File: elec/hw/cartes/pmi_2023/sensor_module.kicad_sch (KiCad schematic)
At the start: 25 parts, among them U12 LSM6DSO32XTR, U22 VL53L5CXV0GC, U30 VL53L5CXV0GC

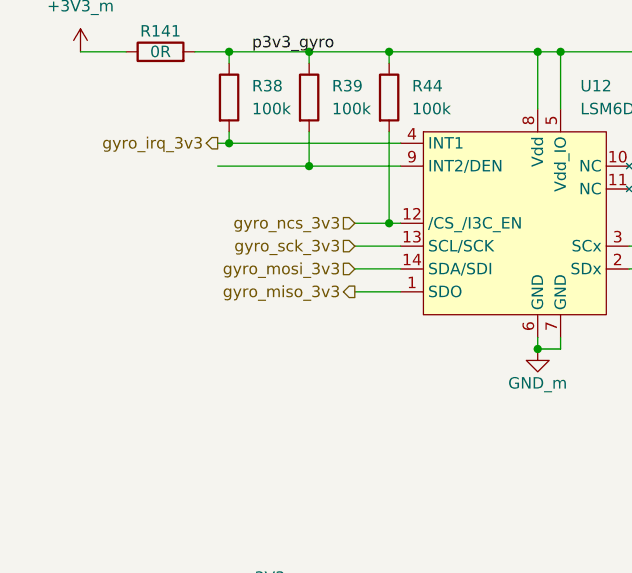
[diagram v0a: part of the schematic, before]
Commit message: GP2S60B replaced by ITR1204SR10A, RGB LED replaced by NH-B2020RGBA
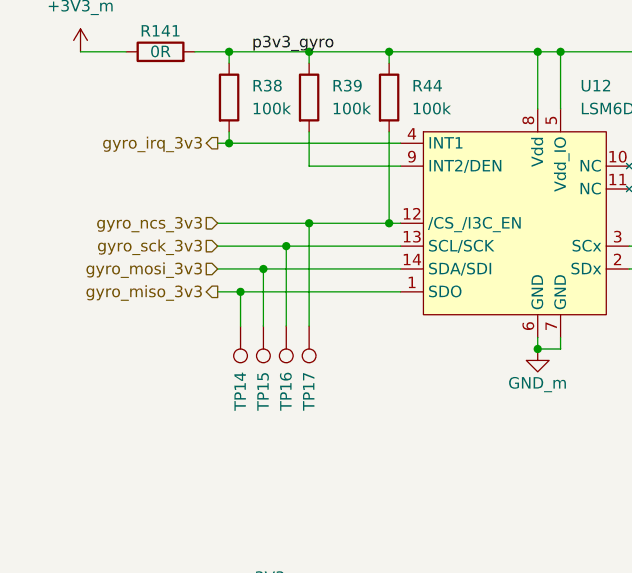
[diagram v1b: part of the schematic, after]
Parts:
- added TP14, TP15, TP16, TP17: TestPoint, cocotter_others:testpoint-THT-0.5mm, symbol cocotter_others:TestPoint
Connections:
- net gyro_miso_3v3: now also TP14.1
- net gyro_mosi_3v3: now also TP15.1
- net gyro_ncs_3v3: now also TP17.1
- net gyro_sck_3v3: now also TP16.1

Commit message: start sensor replaced
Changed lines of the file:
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@@
 					(size 1.27 1.27)
 				)
+				(hide yes)
 			)
 		)
@@
 		(on_board yes)
 		(dnp no)
-		(fields_autoplaced yes)
 		(property "Reference" "U12"
-			(at 73.3141 26.67 0)
+			(at 72.39 30.48 0)
 			(effects
 				(font
@@
 		)
 		(property "Value" "LSM6DSO32XTR"
-			(at 73.3141 29.21 0)
+			(at 72.39 53.34 0)
 			(effects
 				(font
@@
 					(size 1.27 1.27)
 				)
-			)
-		)
+				(hide yes)
+			)
+		)

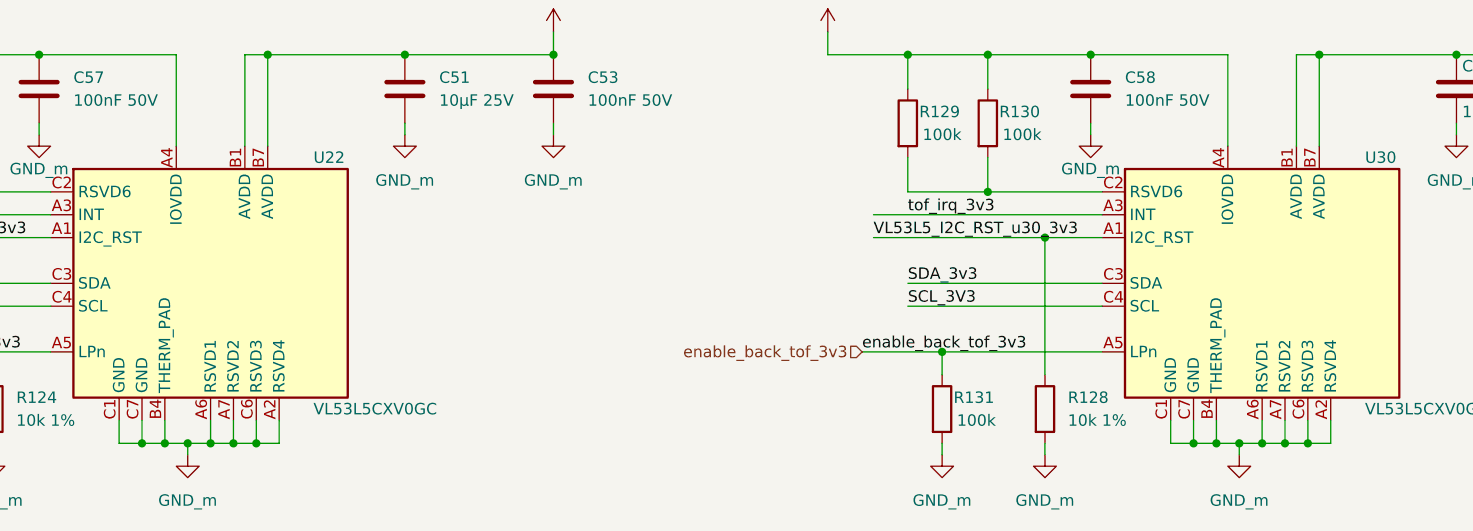
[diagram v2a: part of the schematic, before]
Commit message: XRA1200 replaced by TCA6408
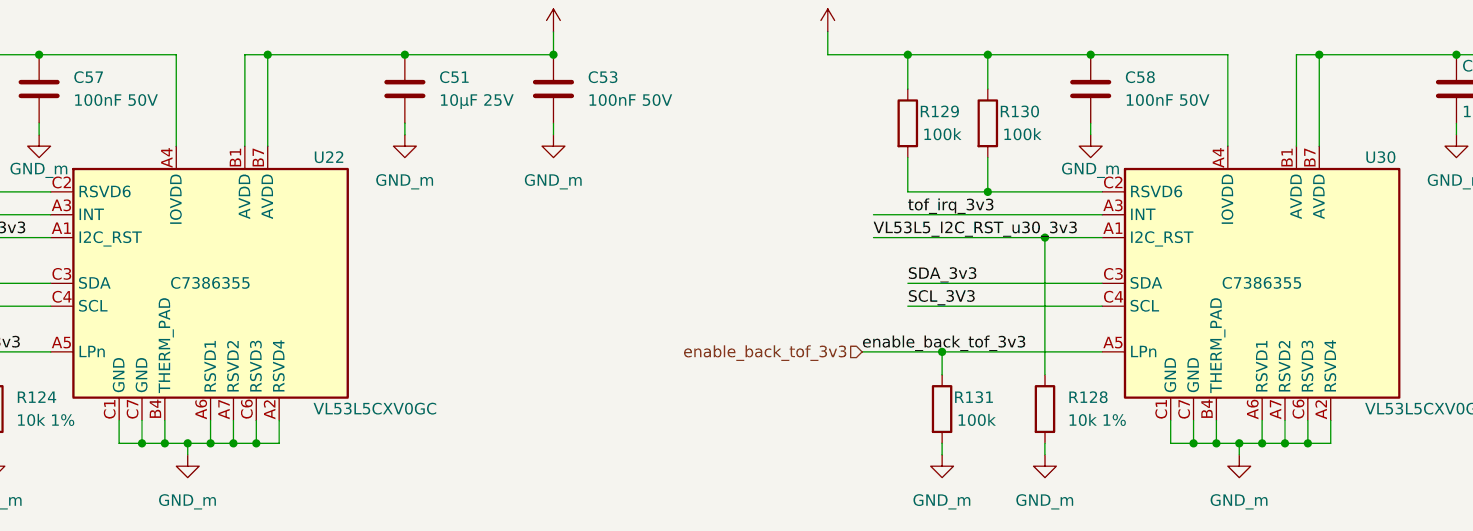
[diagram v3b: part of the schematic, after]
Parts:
- C12, C53, C57, C58, C59: JLCPCB C14663 -> (none); JLCPCB Part # (none) -> C14663
- C51, C52: JLCPCB C15850 -> (none); JLCPCB Part # (none) -> C15850
- R101, R125, R126, R127, R129, R130, R131, R38, R39, R44, R45: JLCPCB C25803 -> (none); JLCPCB Part # (none) -> C25803
- R123, R124, R128: JLCPCB C25804 -> (none); JLCPCB Part # (none) -> C25804
- R141: JLCPCB C431718 -> (none); JLCPCB Part # (none) -> C431718
- U12: JLCPCB C2655100 -> (none); JLCPCB Part # (none) -> C2655100
- U22, U30: JLCPCB C7386355 -> (none); JLCPCB Part # (none) -> C7386355
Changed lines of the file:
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@@
 			)
 		)
-		(property "JLCPCB" "C431718"
+		(property "JLCPCB Part #" "C431718"
 			(at 26.67 22.86 0)
 			(effects
@@
 			)
 		)
-		(property "JLCPCB" "C15850"
+		(property "JLCPCB Part #" "C15850"
 			(at 109.22 92.71 0)
 			(effects
@@
 			)
 		)
-		(property "JLCPCB" "C14663"
+		(property "JLCPCB Part #" "C14663"
 			(at 68.58 92.71 0)
 			(effects
@@
 			)
 		)
-		(property "JLCPCB" "C25803"
+		(property "JLCPCB Part #" "C25803"
 			(at 82.55 39.37 0)
 			(effects
@@
 			)
 		)
-		(property "JLCPCB" "C14663"
+		(property "JLCPCB Part #" "C14663"
 			(at 185.42 92.71 0)
 			(effects
@@
 			)
 		)
-		(property "JLCPCB" "C25803"
+		(property "JLCPCB Part #" "C25803"
 			(at 52.07 27.94 0)
 			(effects
@@
 			)
 		)
-		(property "JLCPCB" "C7386355"
+		(property "JLCPCB Part #" "C7386355"
 			(at 204.47 114.3 0)
 			(effects
@@
 					(size 1.27 1.27)
 				)
-				(hide yes)
 			)
 		)
@@
 			)
 		)
-		(property "JLCPCB" "C25803"
+		(property "JLCPCB Part #" "C25803"
 			(at 57.15 96.52 0)
 			(effects
@@
 			)
 		)
-		(property "JLCPCB" "C15850"
+		(property "JLCPCB Part #" "C15850"
 			(at 226.06 92.71 0)
 			(effects
@@
 			)
 		)
-		(property "JLCPCB" "C14663"
+		(property "JLCPCB Part #" "C14663"
 			(at 242.57 92.71 0)
 			(effects
@@
 			)
 		)
-		(property "JLCPCB" "C25803"
+		(property "JLCPCB Part #" "C25803"
 			(at 173.99 96.52 0)
 			(effects
@@
 			)
 		)
-		(property "JLCPCB" "C2655100"
+		(property "JLCPCB Part #" "C2655100"
 			(at 66.04 41.91 0)
 			(effects
@@
 			)
 		)
-		(property "JLCPCB" "C14663"
+		(property "JLCPCB Part #" "C14663"
 			(at 125.73 92.71 0)
 			(effects
@@
 			)
 		)
-		(property "JLCPCB" "C25803"
+		(property "JLCPCB Part #" "C25803"
 			(at 91.44 39.37 0)
 			(effects
@@
 			)
 		)
-		(property "JLCPCB" "C25803"
+		(property "JLCPCB Part #" "C25803"
 			(at 48.26 96.52 0)
 			(effects
@@
 			)
 		)
-		(property "JLCPCB" "C14663"
+		(property "JLCPCB Part #" "C14663"
 			(at 99.06 26.67 0)
 			(effects
@@
 			)
 		)
-		(property "JLCPCB" "C25803"
+		(property "JLCPCB Part #" "C25803"
 			(at 52.07 128.27 0)
 			(effects
@@
 			)
 		)
-		(property "JLCPCB" "C7386355"
+		(property "JLCPCB Part #" "C7386355"
 			(at 87.63 114.3 0)
 			(effects
@@
 					(size 1.27 1.27)
 				)
-				(hide yes)
 			)
 		)
@@
 			)
 		)
-		(property "JLCPCB" "C25803"
+		(property "JLCPCB Part #" "C25803"
 			(at 168.91 128.27 0)
 			(effects
@@
 			)
 		)
-		(property "JLCPCB" "C25804"
+		(property "JLCPCB Part #" "C25804"
 			(at 63.5 128.27 0)
 			(effects
@@
 			)
 		)
-		(property "JLCPCB" "C25803"
+		(property "JLCPCB Part #" "C25803"
 			(at 34.29 27.94 0)
 			(effects
@@
 			)
 		)
-		(property "JLCPCB" "C25803"
+		(property "JLCPCB Part #" "C25803"
 			(at 165.1 96.52 0)
 			(effects
@@
 			)
 		)
-		(property "JLCPCB" "C25803"
+		(property "JLCPCB Part #" "C25803"
 			(at 43.18 27.94 0)
 			(effects
@@
 			)
 		)
-		(property "JLCPCB" "C25804"
+		(property "JLCPCB Part #" "C25804"
 			(at 39.37 96.52 0)
 			(effects
@@
 			)
 		)
-		(property "JLCPCB" "C25804"
+		(property "JLCPCB Part #" "C25804"
 			(at 180.34 128.27 0)
 			(effects

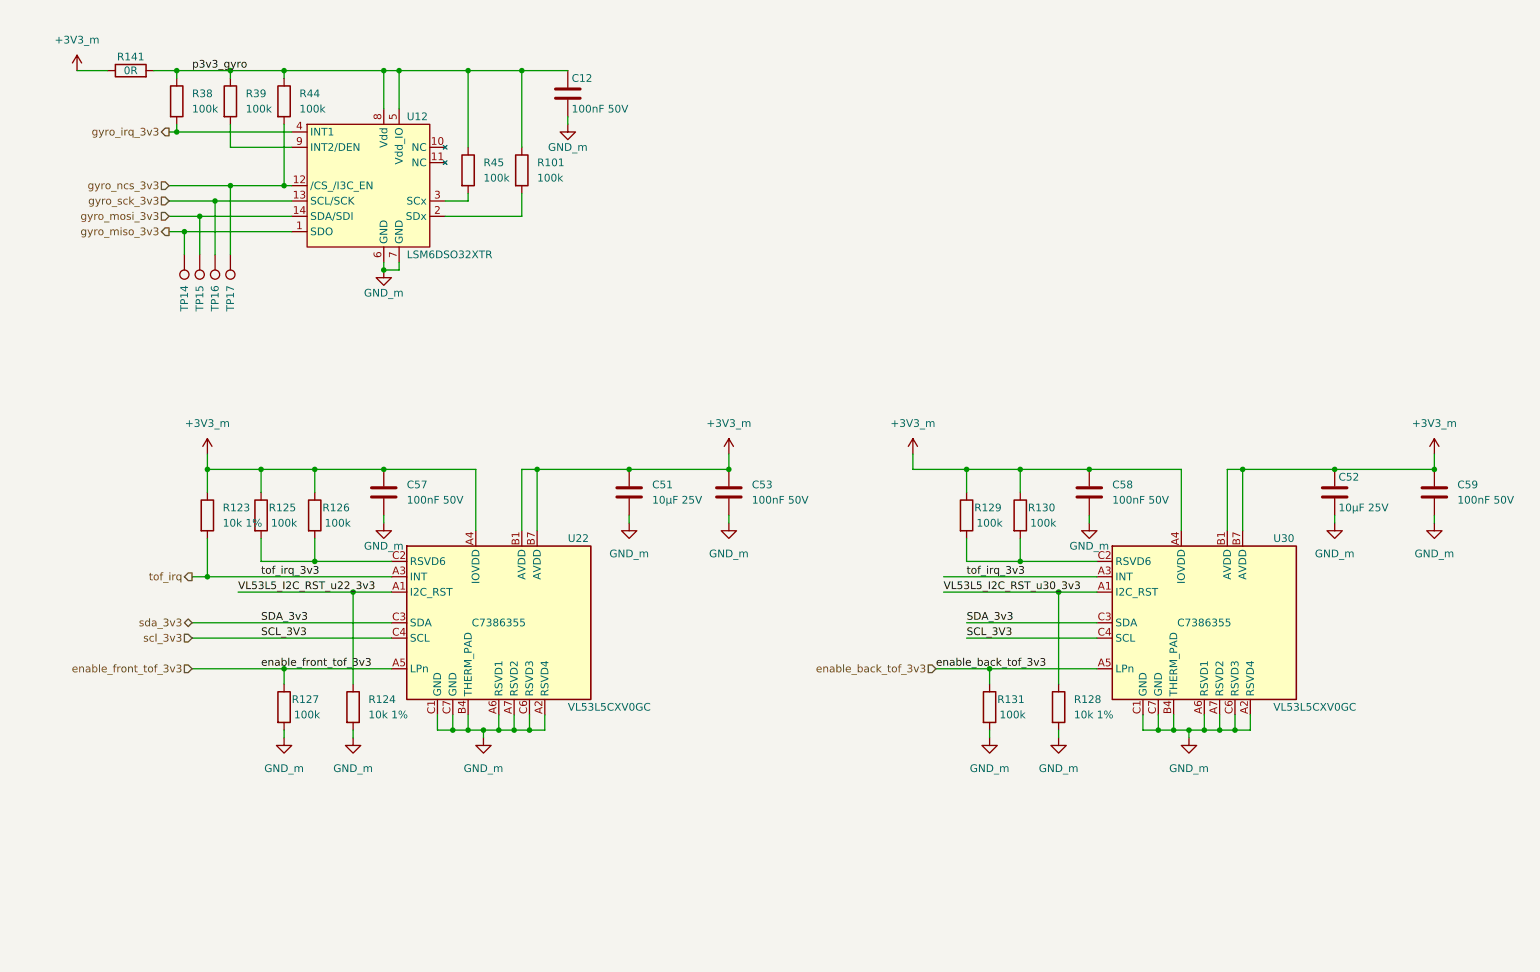
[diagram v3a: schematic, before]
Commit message: bom updated and component selection optimized to decrease bom cost
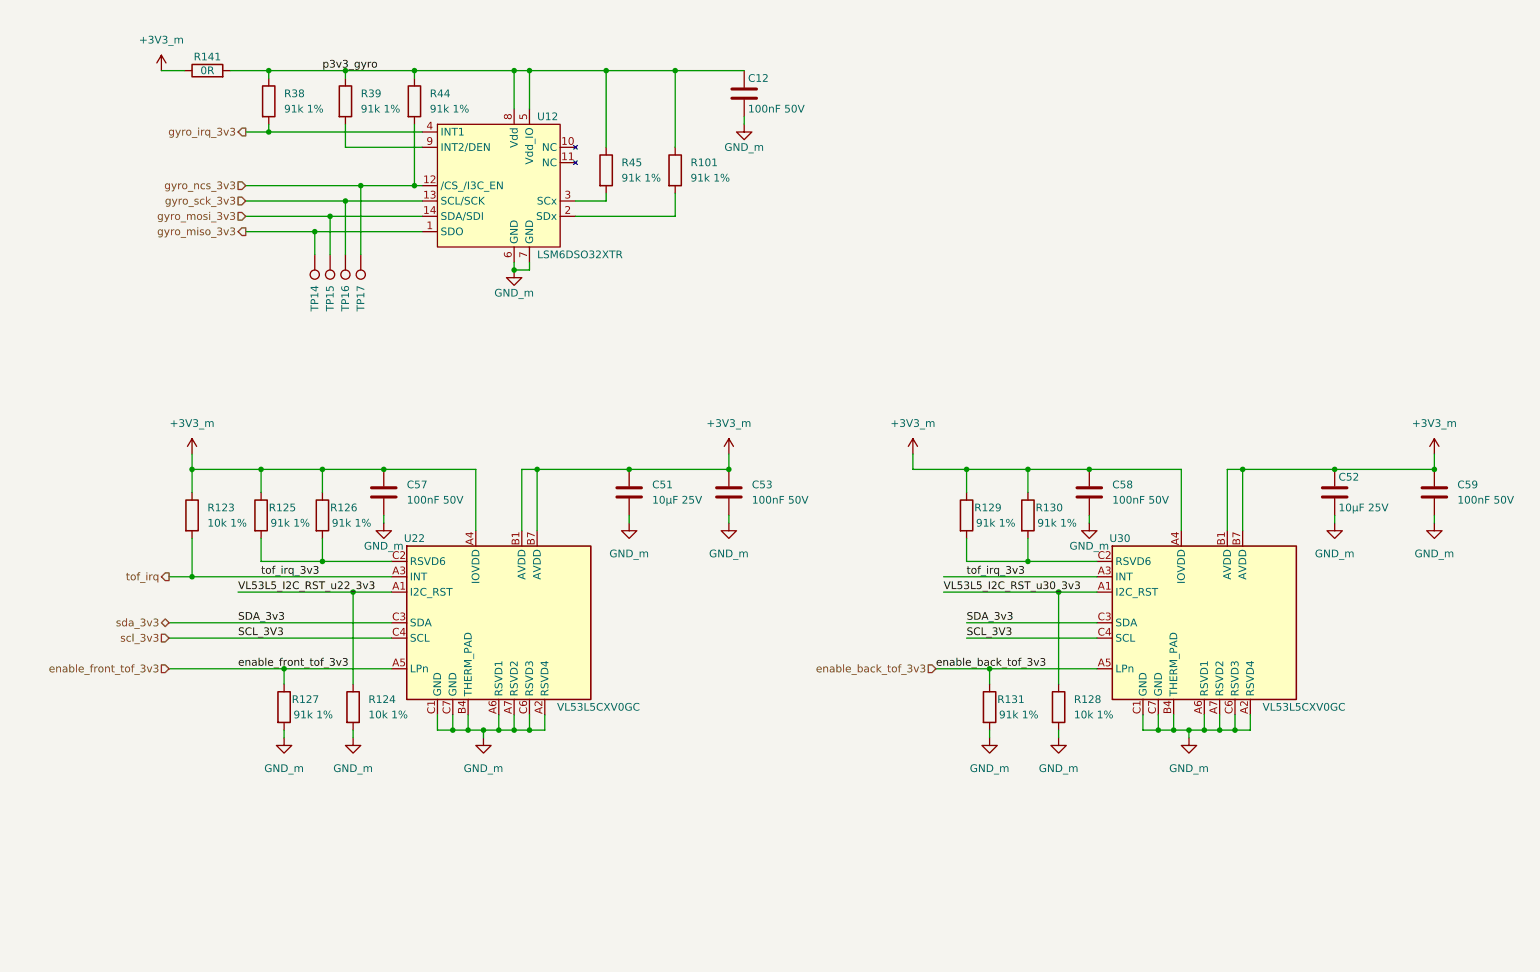
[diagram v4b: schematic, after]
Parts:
- R101, R125, R126, R127, R129, R130, R131, R38, R39, R44, R45: value 100k -> 91k 1%; symbol cocotter_resistors:R_100k_0603_1% -> cocotter_resistors:R_91k_0603_1%; JLCPCB Part # C25803 -> C23265; Specification 100k 0603 1% 100mW -> 91k 0603 1% 100mW; mouser 603-RC0603FR-10100KL -> (none)
- U22, U30: JLCPCB Part # C7386355 -> C3178303
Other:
- moved on the sheet: C12, R101, R123, R126, R130, R141, R38, R39, R44, R45, TP14, TP15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

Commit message: first pass review corrections
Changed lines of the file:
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@@
+		)
+	)
+	(text_box "default I2C@ : 0b0101001"
+		(exclude_from_sim no)
+		(at 156.21 142.24 0)
+		(size 13.97 7.62)
+		(stroke
+			(width 0)
+			(type default)
+		)
+		(fill
+			(type color)
+			(color 0 194 0 1)
+		)
+		(effects
+			(font
+				(size 1.27 1.27)
+			)
+		)
+	)
+	(text_box "default I2C@ : 0b0101001"
+		(exclude_from_sim no)
+		(at 41.91 142.24 0)
+		(size 13.97 7.62)
+		(stroke
+			(width 0)
+			(type default)
+		)
+		(fill
+			(type color)
+			(color 0 194 0 1)
+		)
+		(effects
+			(font
+				(size 1.27 1.27)
+			)
 		)
 	)

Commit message: second round of review corrections
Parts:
- added C20: 100nF 50V, cocotter_capacitors:C_0603_1608Metric, symbol cocotter_capacitors:C_100nF_50V_0603
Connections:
- net +3V3_m: now also C12.1, R101.1, R38.1, R39.1, R44.1, R45.1, U12.5 (Vdd_IO)
- net GND_m: now also C20.2
- removed net p3v3_gyro: C12.1, R101.1, R141.2, R38.1, R39.1, R44.1, R45.1, U12.5 (Vdd_IO), U12.8 (Vdd)
- new net: C20.1, R141.2, U12.8 (Vdd)
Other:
- moved on the sheet: C12, R141

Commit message: pmi board V2, ready for review
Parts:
- U22: now not fitted
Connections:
- net scl_3v3 renamed scl_tof_3v3
- net sda_3v3 renamed sda_tof_3v3
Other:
- note added: "Back multizone TOF sensor"
- note added: "Front multizone TOF sensor"
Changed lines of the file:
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@@
 		)
 	)
-	(label "SDA_3v3"
+	(text "Front multizone TOF sensor"
+		(exclude_from_sim no)
+		(at 32.512 74.93 0)
+		(effects
+			(font
+				(size 1.27 1.27)
+			)
+		)
+	)
+	(text "Back multizone TOF sensor"
+		(exclude_from_sim no)
+		(at 151.892 74.676 0)
+		(effects
+			(font
+				(size 1.27 1.27)
+				(thickness 0.254)
+				(bold yes)
+			)
+			(justify left bottom)
+		)
+	)
+	(label "sda_tof_3v3"
 		(at 165.1 114.3 0)
-		(fields_autoplaced yes)
 		(effects
 			(font
@@
 	(label "tof_irq_3v3"
 		(at 48.26 106.68 0)
-		(fields_autoplaced yes)
 		(effects
 			(font
@@
 		)
 	)
-	(label "SDA_3v3"
+	(label "sda_tof_3v3"
 		(at 44.45 114.3 0)
-		(fields_autoplaced yes)
 		(effects
 			(font
@@
 		)
 	)
-	(label "SCL_3V3"
+	(label "scl_tof_3v3"
 		(at 44.45 116.84 0)
-		(fields_autoplaced yes)
 		(effects
 			(font
@@
 	(label "VL53L5_I2C_RST_u22_3v3"
 		(at 44.45 109.22 0)
-		(fields_autoplaced yes)
 		(effects
 			(font
@@
 		)
 	)
-	(label "SCL_3V3"
+	(label "scl_tof_3v3"
 		(at 165.1 116.84 0)
-		(fields_autoplaced yes)
 		(effects
 			(font
@@
 	(label "enable_front_tof_3v3"
 		(at 44.45 121.92 0)
-		(fields_autoplaced yes)
 		(effects
 			(font
@@
 	(label "p3v3_gyro"
 		(at 58.42 22.86 0)
-		(fields_autoplaced yes)
 		(effects
 			(font
@@
 	(label "enable_back_tof_3v3"
 		(at 160.02 121.92 0)
-		(fields_autoplaced yes)
 		(effects
 			(font
@@
 	(label "VL53L5_I2C_RST_u30_3v3"
 		(at 161.29 109.22 0)
-		(fields_autoplaced yes)
 		(effects
 			(font
@@
 	(label "tof_irq_3v3"
 		(at 165.1 106.68 0)
-		(fields_autoplaced yes)
 		(effects
 			(font
@@
 		(shape output)
 		(at 45.72 49.53 180)
-		(fields_autoplaced yes)
 		(effects
 			(font
@@
 		(shape input)
 		(at 45.72 41.91 180)
-		(fields_autoplaced yes)
 		(effects
 			(font
@@
 		)
 	)
-	(hierarchical_label "scl_3v3"
+	(hierarchical_label "scl_tof_3v3"
 		(shape input)
 		(at 33.02 116.84 180)
-		(fields_autoplaced yes)
 		(effects
 			(font
@@
 		(shape input)
 		(at 160.02 121.92 180)
-		(fields_autoplaced yes)
 		(effects
 			(font
@@
 		(shape output)
 		(at 33.02 106.68 180)
-		(fields_autoplaced yes)
 		(effects
 			(font
@@
 		(shape output)
 		(at 45.72 33.02 180)
-		(fields_autoplaced yes)
 		(effects
 			(font
@@
 		(shape input)
 		(at 45.72 46.99 180)
-		(fields_autoplaced yes)
 		(effects
 			(font
@@
 		)
 	)
-	(hierarchical_label "sda_3v3"
+	(hierarchical_label "sda_tof_3v3"
 		(shape bidirectional)
 		(at 33.02 114.3 180)
-		(fields_autoplaced yes)
 		(effects
 			(font
@@
 		(shape input)
 		(at 45.72 44.45 180)
-		(fields_autoplaced yes)
 		(effects
 			(font
@@
 		(shape input)
 		(at 33.02 121.92 180)
-		(fields_autoplaced yes)
 		(effects
 			(font
@@
 		(in_bom yes)
 		(on_board yes)
-		(dnp no)
+		(dnp yes)
 		(property "Reference" "U22"
 			(at 73.66 100.33 0)
